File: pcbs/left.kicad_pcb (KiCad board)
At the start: 2 copper layers, 123.1 x 93.2 mm, 28 parts

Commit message: Update battery label
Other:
- board text added: "602030 Battery"
- board text removed: "XX2030 Battery"
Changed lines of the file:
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@@
   (title_block
     (title "left")
-    (date "2024-12-06")
+    (date "2024-12-10")
     (rev "v1.0.0")
     (company "Unknown")
@@
     (segment (start 101.49850682877624 112.23429119999996) (end 99.69850682877625 112.23429119999996) (width 0.25) (layer "F.Cu") (net 54))
     (segment (start 101.49850682877624 112.23429119999996) (end 99.69850682877625 112.23429119999996) (width 0.25) (layer "B.Cu") (net 54))
-  (gr_text "XX2030 Battery"
+  (gr_text "602030 Battery"
     (at 118.1483666 94.68429119999999 0)
     (layer "F.SilkS" )
@@
     )
   )
-  (gr_text "XX2030 Battery"
+  (gr_text "602030 Battery"
     (at 118.1483666 94.68429119999999 0)
     (layer "B.SilkS" )

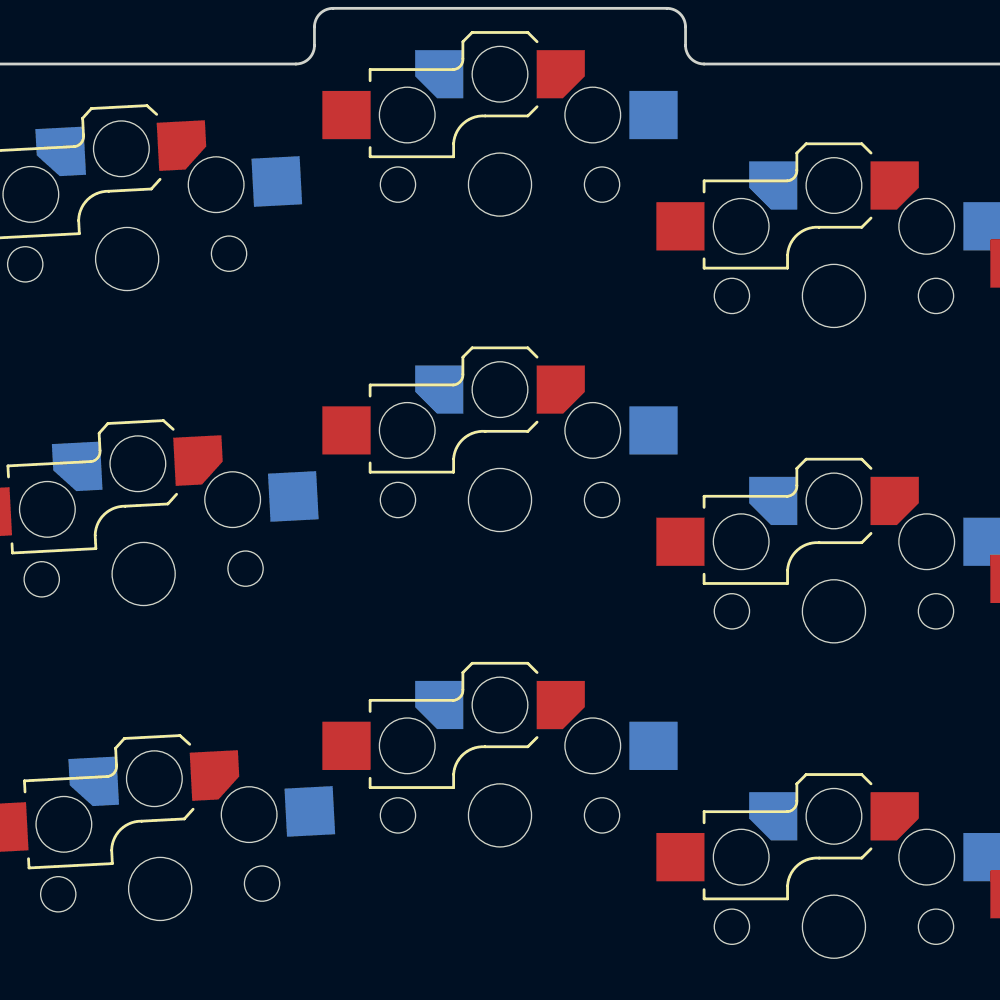
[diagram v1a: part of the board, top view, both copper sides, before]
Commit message: Add tenting puck, need to test in KiCad
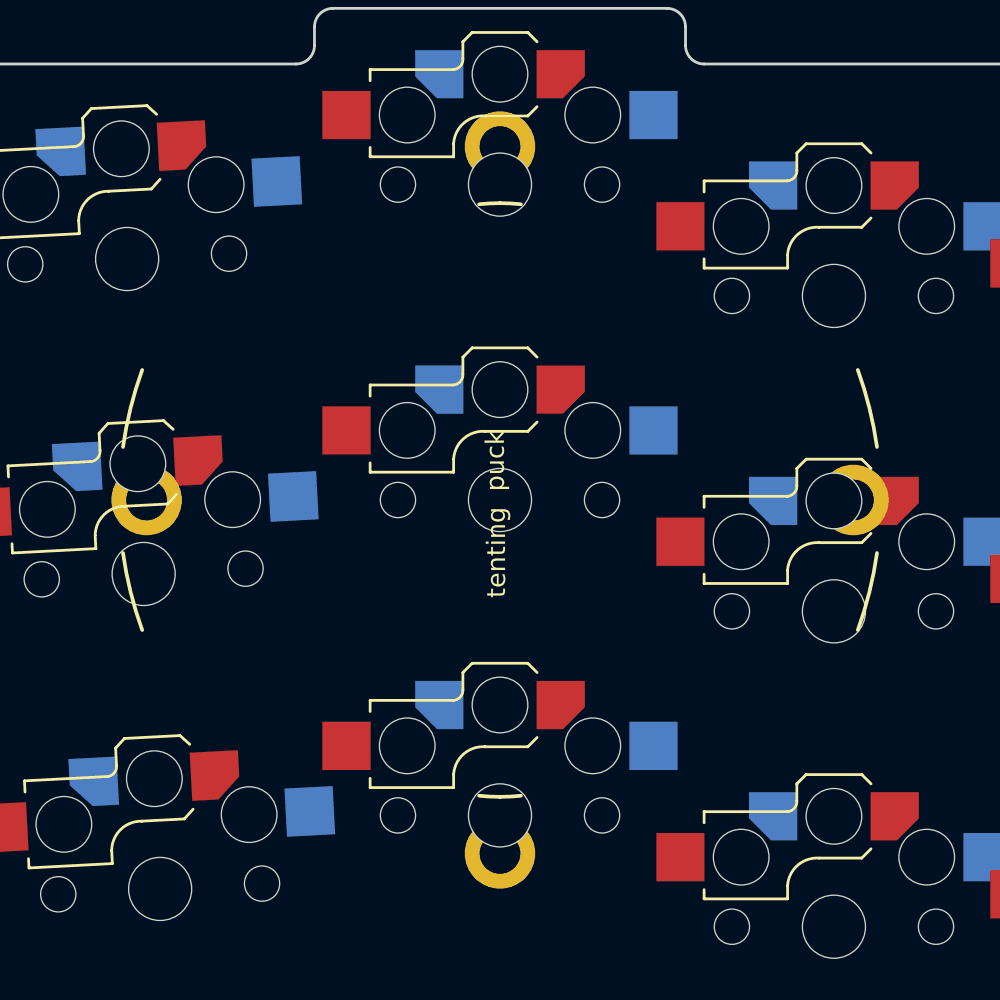
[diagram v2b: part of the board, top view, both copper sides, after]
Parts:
- added TENTINGPUCK1: Tenting Puck, TentingPuck, F.Cu at (135.1, 62.2)

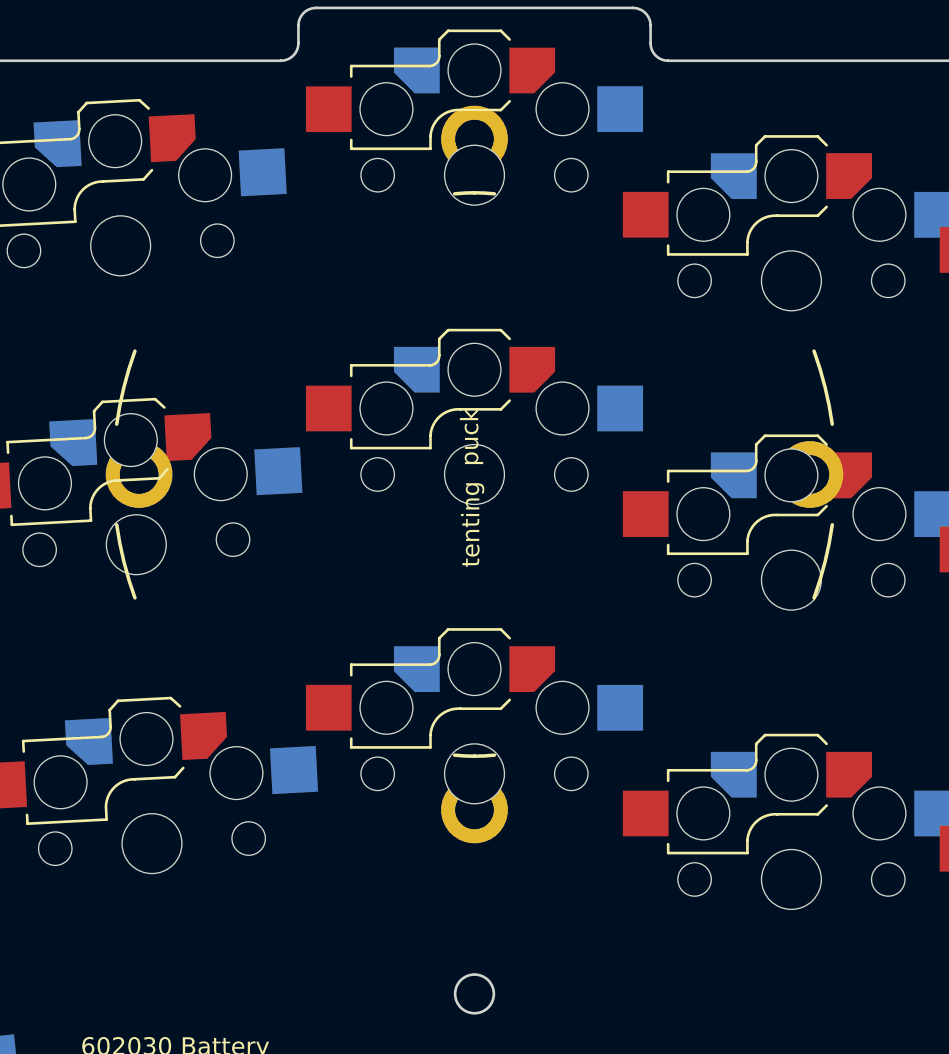
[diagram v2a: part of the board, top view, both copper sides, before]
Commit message: Shift puck down and try rotating it
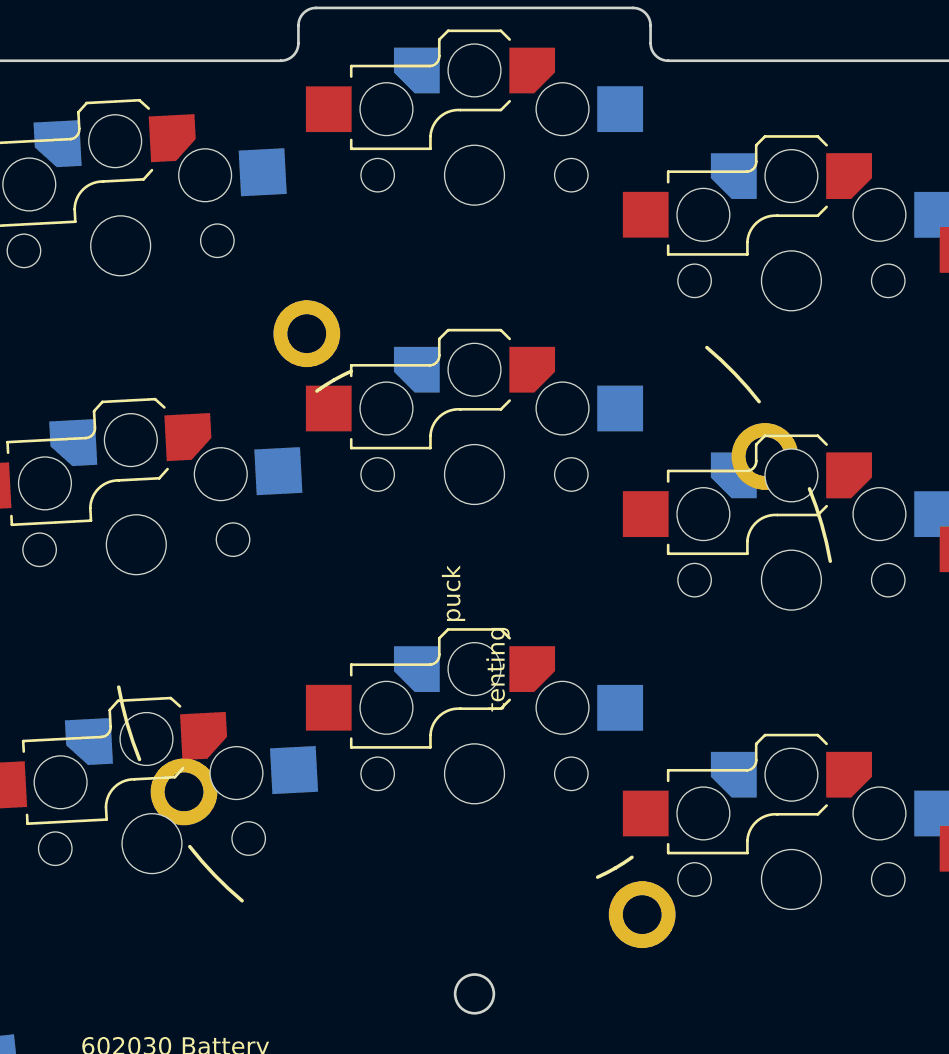
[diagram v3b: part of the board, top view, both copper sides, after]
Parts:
- moved TENTINGPUCK1 8.50 mm to (135.1, 70.7), turned to 30 degrees
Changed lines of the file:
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@@
 	(generator_version "8.0")
 	(layer "F.Cu")
-  (at 135.1483667 62.18429119999999 0)
+  (at 135.1483667 70.68429119999999 30)
 	(property "Reference" "TENTINGPUCK1"
 		(at 0 0 0)

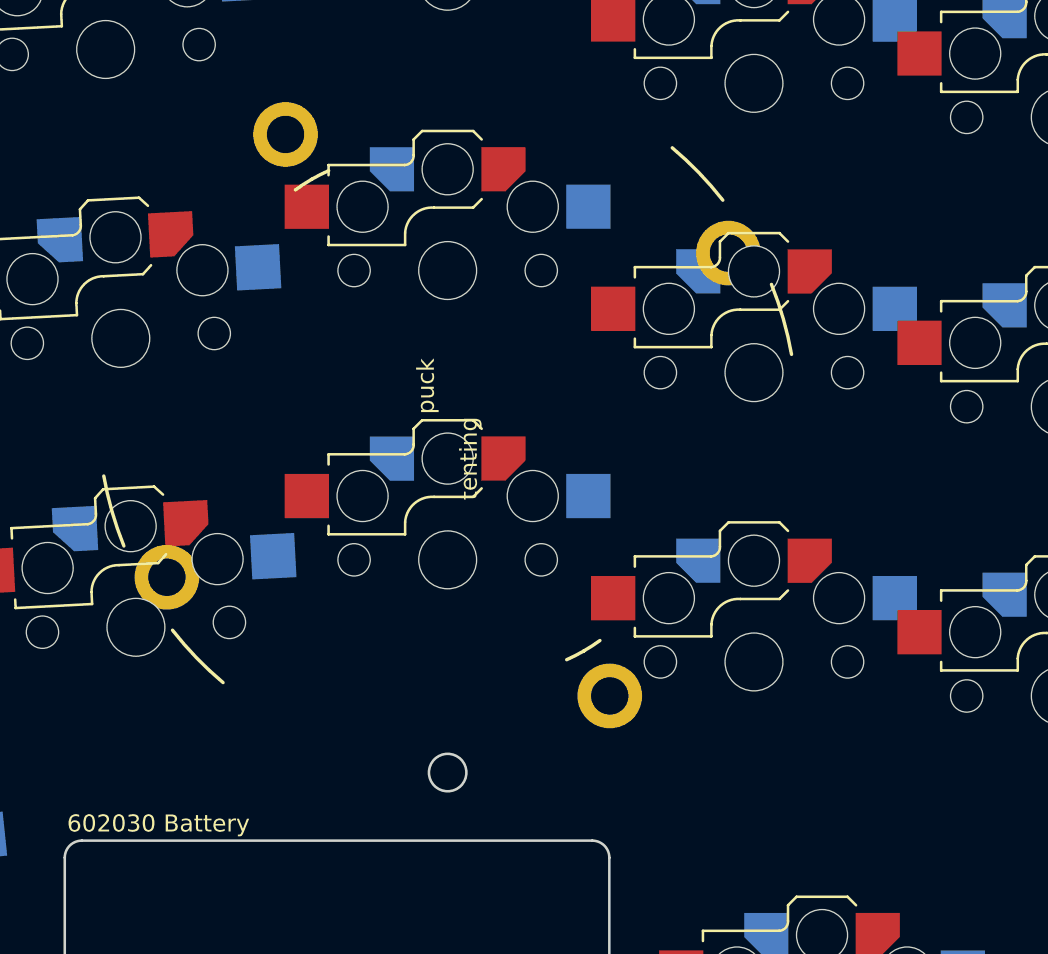
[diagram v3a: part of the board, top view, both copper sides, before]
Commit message: Move tenting puck a little towards pointer
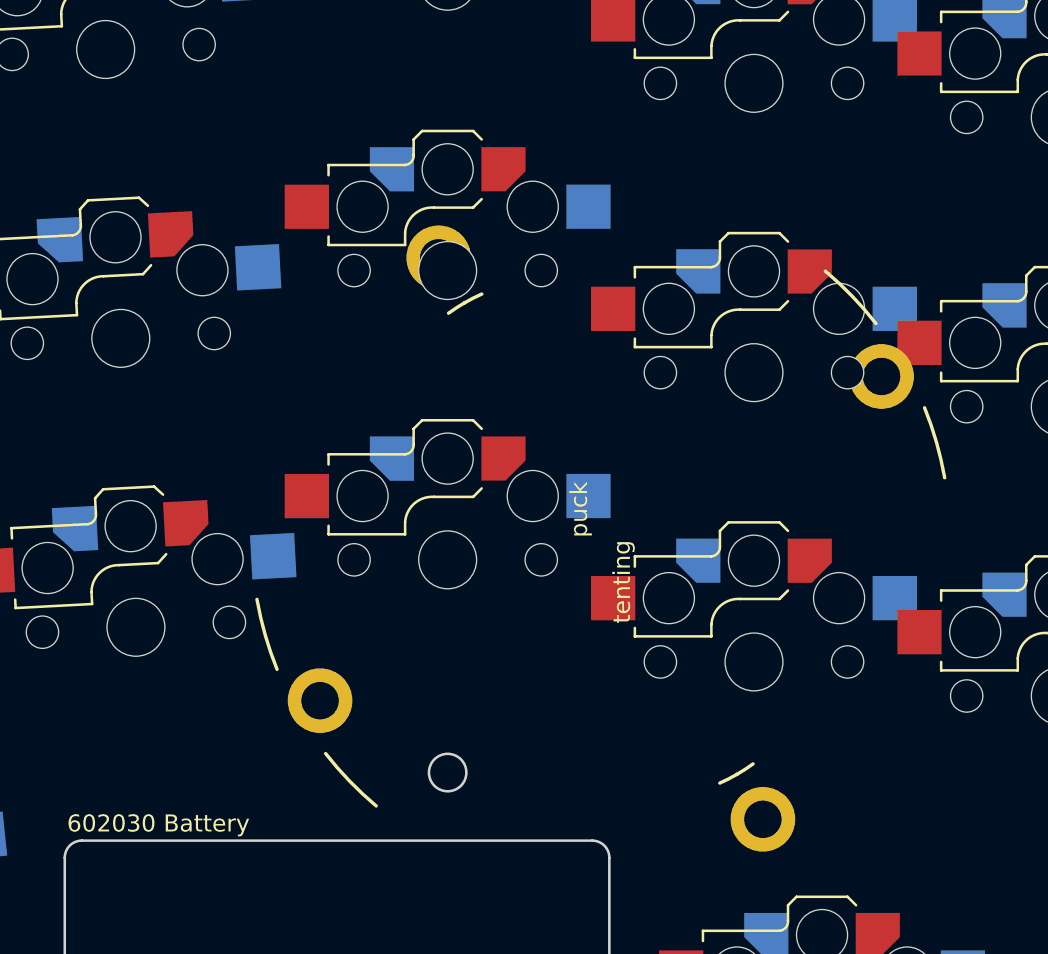
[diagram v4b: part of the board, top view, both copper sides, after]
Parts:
- moved TENTINGPUCK1 11.6 mm to (144.1, 77.9)
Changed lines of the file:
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@@
 	(generator_version "8.0")
 	(layer "F.Cu")
-  (at 135.1483667 70.68429119999999 30)
+  (at 144.14836665 77.93429119999999 30)
 	(property "Reference" "TENTINGPUCK1"
 		(at 0 0 0)

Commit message: Tweak
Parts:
- moved TENTINGPUCK1 3.85 mm to (141.1, 75.5), turned to 45 degrees
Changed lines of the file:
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@@
 	(generator_version "8.0")
 	(layer "F.Cu")
-  (at 144.14836665 77.93429119999999 30)
+  (at 141.14836666666667 75.51762453333332 45)
 	(property "Reference" "TENTINGPUCK1"
 		(at 0 0 0)

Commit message: Dial it in
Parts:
- moved TENTINGPUCK1 3.16 mm to (142.1, 72.5), turned to -6 degrees
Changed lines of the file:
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@@
 	(generator_version "8.0")
 	(layer "F.Cu")
-  (at 141.14836666666667 75.51762453333332 45)
+  (at 142.14836666666667 72.51762453333332 -6)
 	(property "Reference" "TENTINGPUCK1"
 		(at 0 0 0)

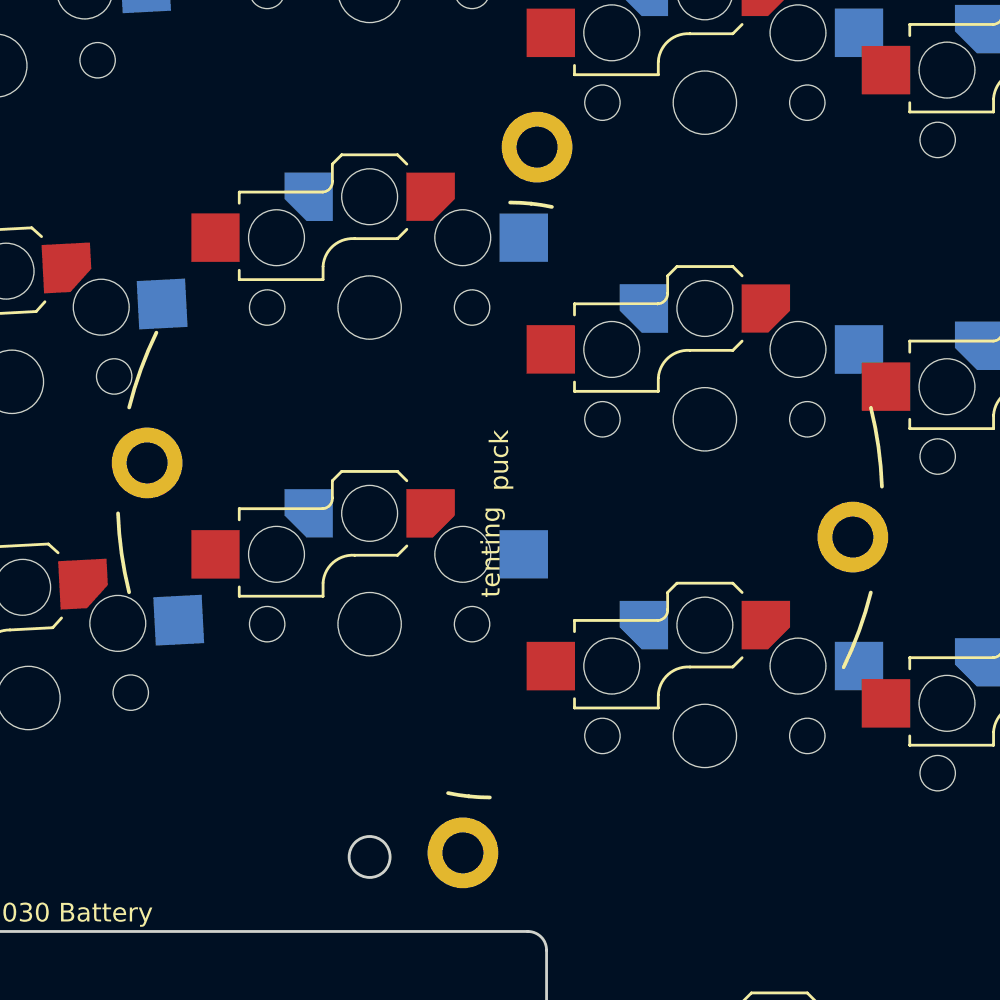
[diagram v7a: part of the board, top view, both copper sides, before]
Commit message: Updated PCB, but this is still WIP
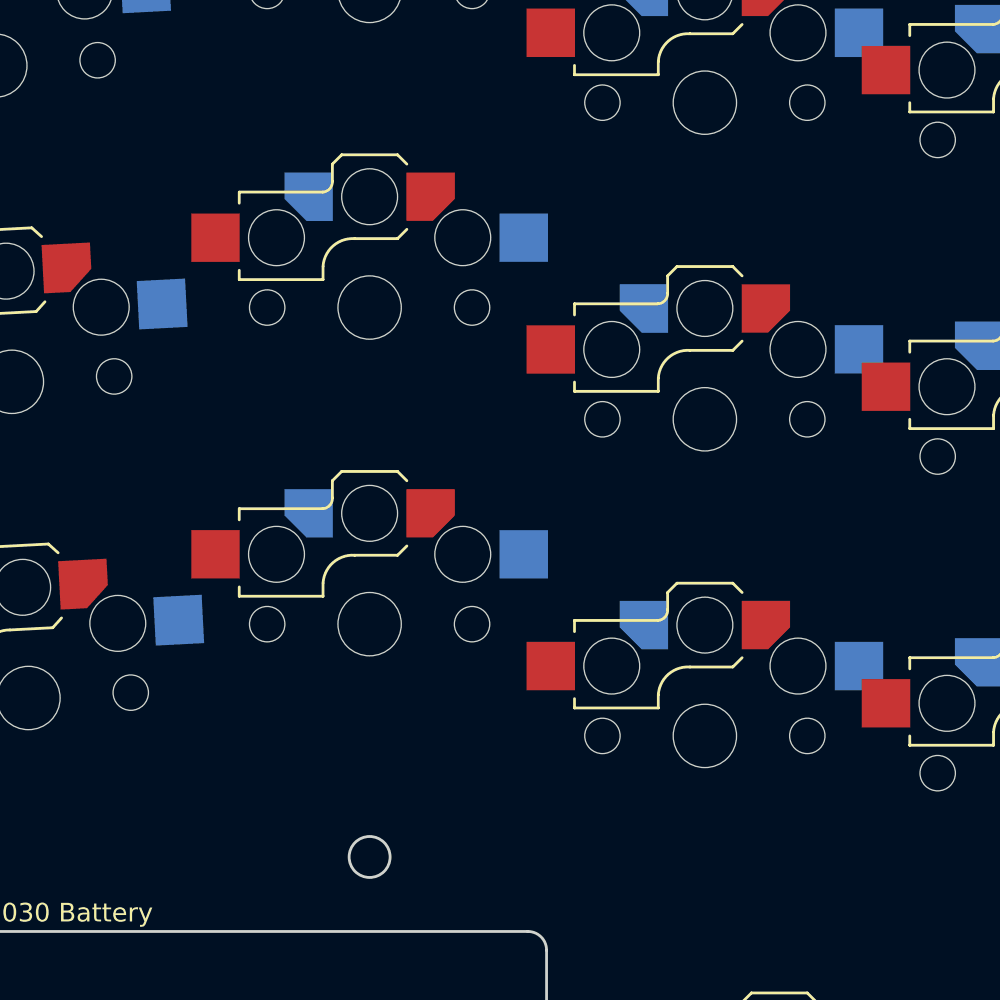
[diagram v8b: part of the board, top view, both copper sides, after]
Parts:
- removed TENTINGPUCK1: Tenting Puck, TentingPuck
